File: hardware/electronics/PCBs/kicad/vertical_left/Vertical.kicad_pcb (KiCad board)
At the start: 2 copper layers, 53.9 x 47.1 mm, 40 parts

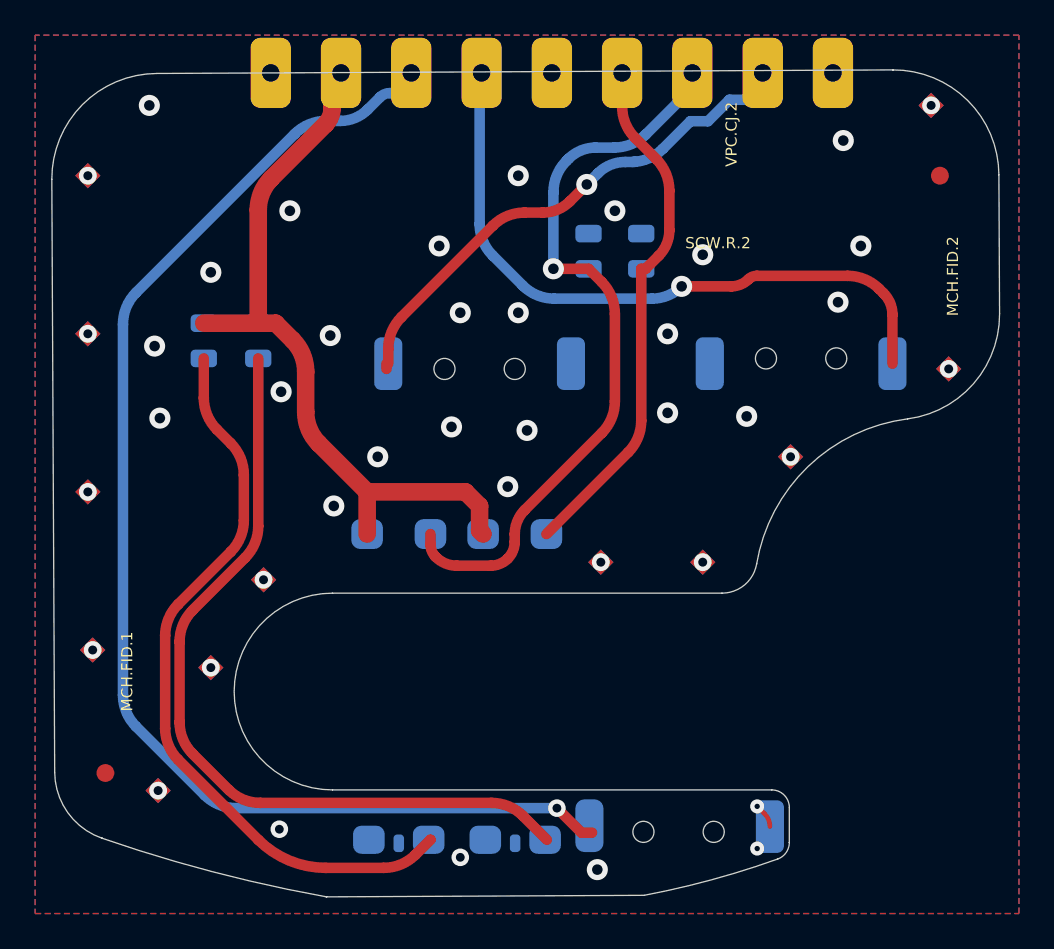
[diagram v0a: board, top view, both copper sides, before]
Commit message: Vertical portion flipped
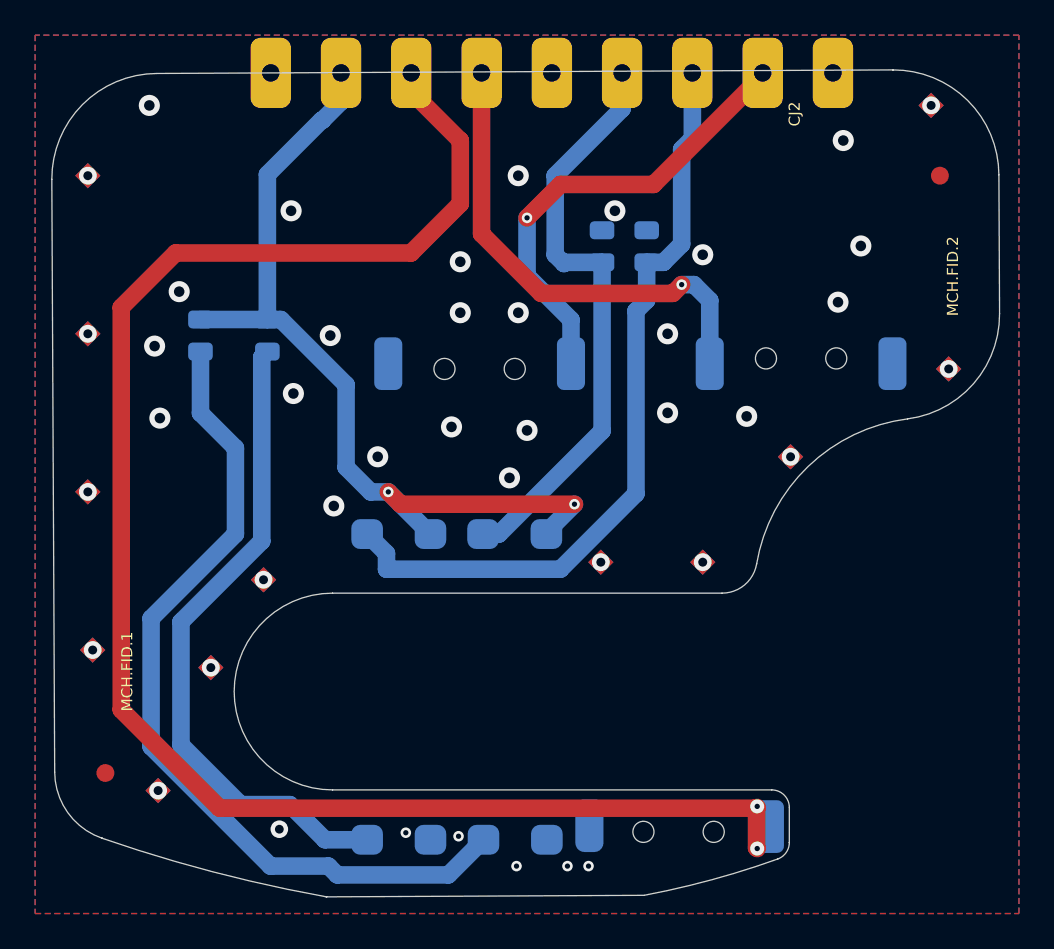
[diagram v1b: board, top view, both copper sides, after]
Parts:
- removed SCW.R.1, SCW.R.2, SCW.R.3, SCW.R.4: 0805, Chip_Passives:0805
- added R1: 100, Resistor_SMD:R_0805_2012Metric, B.Cu at (130.0, 96.6)
- added R2: 1k, Resistor_SMD:R_0805_2012Metric, B.Cu at (155.4, 91.5)
- added R3: 100, Resistor_SMD:R_0805_2012Metric, B.Cu at (133.8, 96.6)
- added R4: 1k, Resistor_SMD:R_0805_2012Metric, B.Cu at (152.8, 91.5)
- D1: renamed from SCW.D.1; footprint LEDs:TR8 -> Library:TR8
- D2: renamed from SCW.D.2; footprint LEDs:TR8 -> Library:TR8
- renumbered VPC.CJ.1 to CJ1, VPC.CJ.2 to CJ2, VPC.CJ.3 to CJ3, VPC.CJ.4 to CJ4, VPC.CJ.5 to CJ5, VPC.CJ.6 to CJ6, VPC.CJ.7 to CJ7, VPC.CJ.8 to CJ8, VPC.CJ.9 to CJ9, SCW.Qt.1 to Qt1, SCW.Qt.2 to Qt2, BBS.SW.1 to SW1, BBS.SW.2 to SW2, SCW.SW.3 to SW3
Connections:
- net NetBBS.SW.1_A renamed /BBS/ButtonLeftClick
- net NetBBS.SW.2_A renamed /BBS/ButtonRightClick
- net NetSCW.Qt.1_E renamed /SCW/ScrollWheelOpto0
- net NetSCW.SW.3_A renamed /SCW/ButtonScrollWheel
- CJ4 pad 1: NetSCW.Qt.2_E -> /SCW/ScrollWheelOpto1
- CJ8 pad 1: 3V3 -> /SCW/3V3
- Qt1 pad C: 3V3 -> /SCW/3V3
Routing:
- net /SCW/3V3: track 0.00 -> 50.0 mm, vias 0 -> 2
- net Net-(D1-A): track 0.00 -> 47.6 mm
- net NetSCW.D.1_A: track 46.2 -> 0.00 mm
- net NetSCW.D.2_A: track 42.5 -> 0.00 mm
- net 3V3: track 41.3 -> 0.00 mm
- net Net-(D2-A): track 0.00 -> 37.3 mm
- net /SCW/ScrollWheelOpto1: track 0.00 -> 33.6 mm
- net NetSCW.Qt.2_E: track 28.9 -> 0.00 mm
- net /BBS/ButtonRightClick: track 74.9 -> 94.1 mm, vias 3 -> 2
- net /BBS/ButtonLeftClick: track 37.5 -> 27.7 mm
- net /SCW/ScrollWheelOpto0: track 41.9 -> 44.3 mm, vias 1 -> 0
- net /SCW/ButtonScrollWheel: track 28.6 -> 26.2 mm
- net GND: vias 39 -> 42
